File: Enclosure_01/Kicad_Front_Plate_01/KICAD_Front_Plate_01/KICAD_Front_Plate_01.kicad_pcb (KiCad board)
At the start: 2 copper layers, 124.8 x 50.9 mm, 0 parts

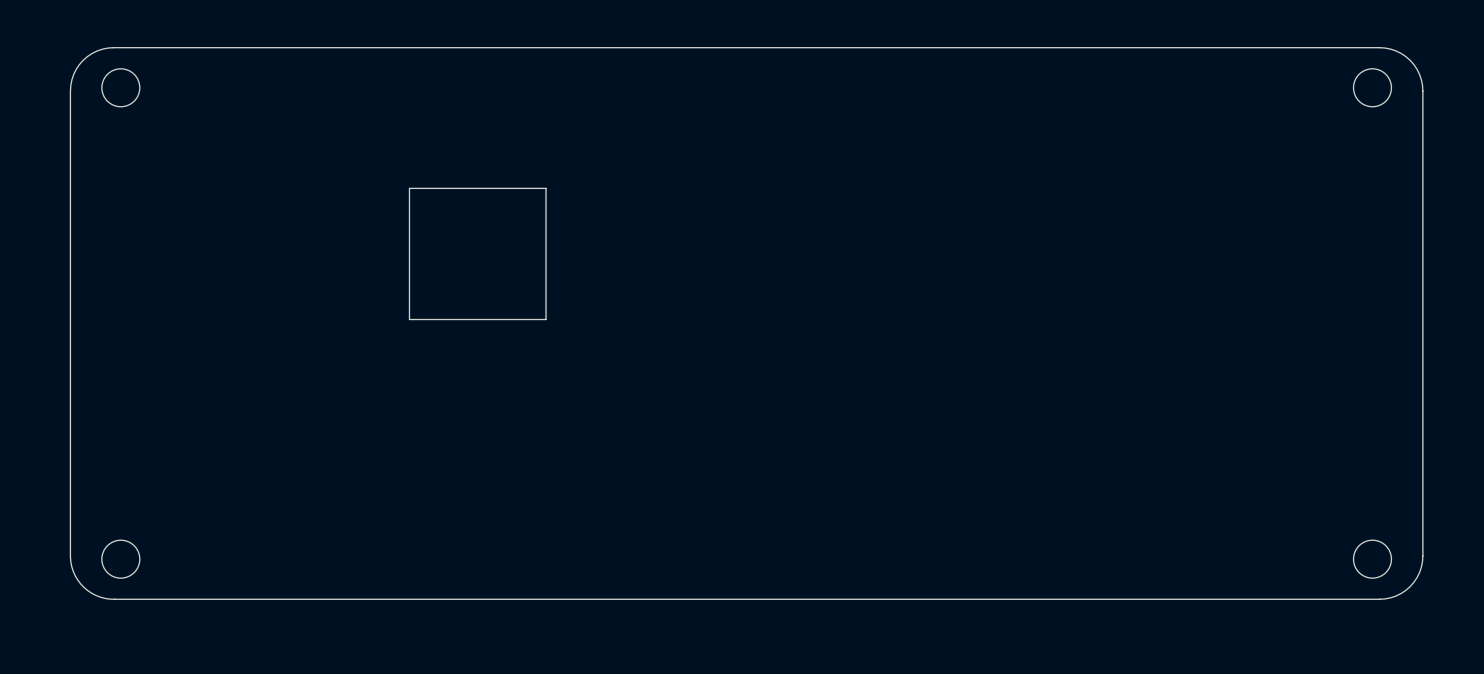
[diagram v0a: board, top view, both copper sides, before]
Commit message: Added masks to Kicad Front/back plates
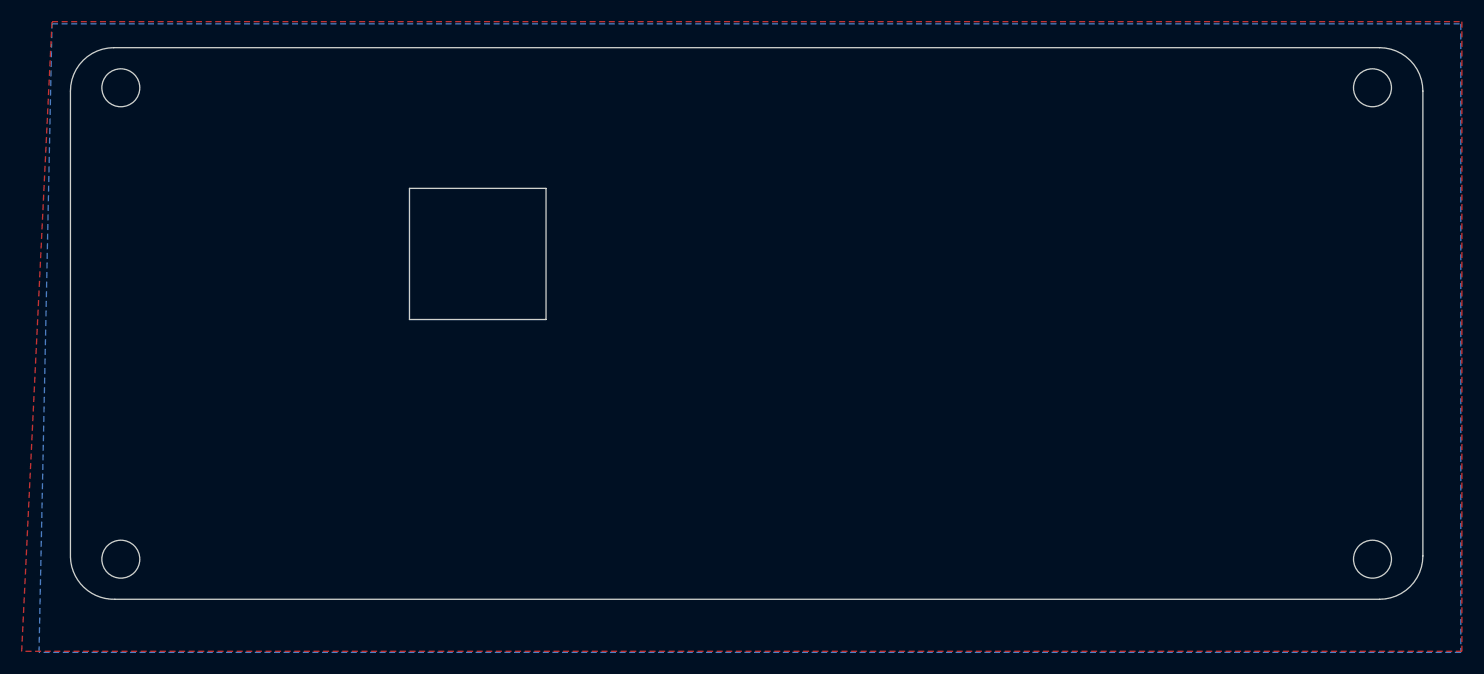
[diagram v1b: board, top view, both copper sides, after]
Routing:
- added copper zone on B.Cu, net (none)
- added copper zone on F.Cu, net (none)
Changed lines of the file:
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@@
   (gr_circle (center 120.15 3.7) (end 121.9 3.7) (layer Edge.Cuts) (width 0.05))
   (gr_circle (center 4.65 47.2) (end 6.4 47.2) (layer Edge.Cuts) (width 0.05))
+  (zone (net 0) (net_name "") (layer F.Cu) (hatch edge 0.508)
+    (connect_pads (clearance 0.508))
+    (min_thickness 0.254)
+    (fill yes (arc_segments 32) (thermal_gap 0.508) (thermal_bridge_width 0.508))
+    (polygon
+      (pts
+        (xy 128.4 55.7) (xy -4.5 55.7) (xy -1.7 -2.4) (xy 128.4 -2.4)
+      )
+    )
+  )
+  (zone (net 0) (net_name "") (layer B.Cu) (hatch edge 0.508)
+    (connect_pads (clearance 0.508))
+    (min_thickness 0.254)
+    (fill yes (arc_segments 32) (thermal_gap 0.508) (thermal_bridge_width 0.508))
+    (polygon
+      (pts
+        (xy 128.3 55.8) (xy -2.9 55.8) (xy -1.7 -2.2) (xy 128.3 -2.2)
+      )
+    )
+  )
 )

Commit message: Updated mounting holes for Copper Plane and Gerber
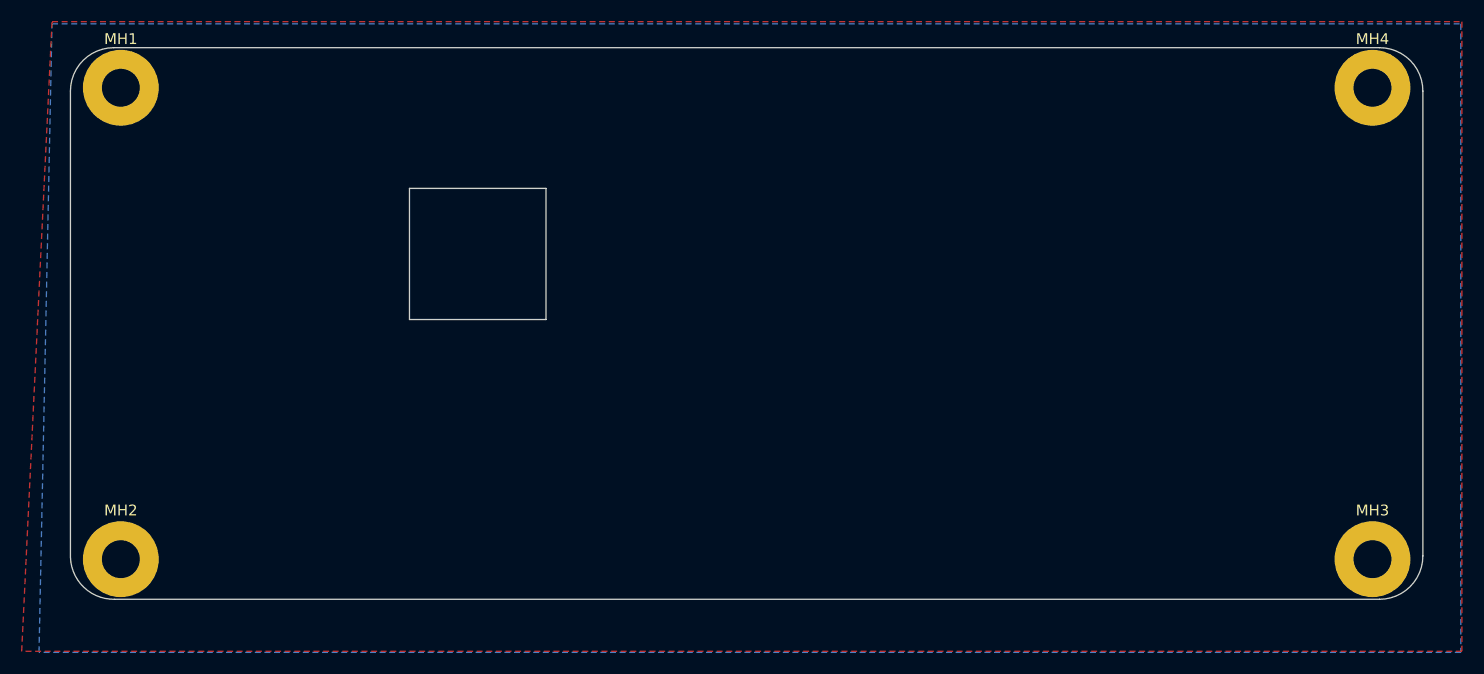
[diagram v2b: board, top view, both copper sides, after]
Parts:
- added MH1: MountingHole, MountingHole:MountingHole_3.5mm_Pad, F.Cu at (4.65, 3.70)
- added MH2: MountingHole, MountingHole:MountingHole_3.5mm_Pad, F.Cu at (4.65, 47.2)
- added MH3: MountingHole, MountingHole:MountingHole_3.5mm_Pad, F.Cu at (120.2, 47.2)
- added MH4: MountingHole, MountingHole:MountingHole_3.5mm_Pad, F.Cu at (120.2, 3.70)
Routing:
- net GND: track 0.00 -> 1.57 mm
- added copper zone on B.Cu, net GND
- added copper zone on F.Cu, net GND
- removed copper zone on B.Cu, net (none)
- removed copper zone on F.Cu, net (none)
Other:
- outline, holes or cut-outs redrawn
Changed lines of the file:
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@@
   (general
     (thickness 1.6)
-    (drawings 16)
-    (tracks 0)
+    (drawings 12)
+    (tracks 3)
     (zones 0)
-    (modules 0)
-    (nets 1)
+    (modules 4)
+    (nets 2)
   )
   (page A4)
@@
     (mod_text_size 1 1)
     (mod_text_width 0.15)
-    (pad_size 1.524 1.524)
-    (pad_drill 0.762)
+    (pad_size 7 7)
+    (pad_drill 3.5)
     (pad_to_mask_clearance 0)
     (aux_axis_origin 0 0)
@@
     (pcbplotparams
       (layerselection 0x010fc_ffffffff)
-      (usegerberextensions false)
-      (usegerberattributes true)
-      (usegerberadvancedattributes true)
-      (creategerberjobfile true)
+      (usegerberextensions true)
+      (usegerberattributes false)
+      (usegerberadvancedattributes false)
+      (creategerberjobfile false)
       (excludeedgelayer true)
       (linewidth 0.100000)
@@
       (psa4output false)
       (plotreference true)
-      (plotvalue true)
+      (plotvalue false)
       (plotinvisibletext false)
       (padsonsilk false)
-      (subtractmaskfromsilk false)
+      (subtractmaskfromsilk true)
       (outputformat 1)
       (mirror false)
@@
   )
   (net 0 "")
+  (net 1 GND)
   (net_class Default "This is the default net class."
     (clearance 0.2)
@@
     (uvia_dia 0.3)
     (uvia_drill 0.1)
+    (add_net GND)
+  )
+  (module MountingHole:MountingHole_3.5mm_Pad (layer F.Cu)
+    (at 4.65 3.7)
+    (descr "Mounting Hole 3.5mm")
+    (tags "mounting hole 3.5mm")
+    (attr virtual)
+    (fp_text reference MH1 (at 0 -4.5) (layer F.SilkS)
+      (effects (font (size 1 1) (thickness 0.15)))
+    )
+    (fp_text value MountingHole (at 0 4.5) (layer F.Fab)
+      (effects (font (size 1 1) (thickness 0.15)))
+    )
+    (fp_circle (center 0 0) (end 3.75 0) (layer F.CrtYd) (width 0.05))
+    (fp_circle (center 0 0) (end 3.5 0) (layer Cmts.User) (width 0.15))
+    (fp_text user %R (at 0.3 0) (layer F.Fab)
+      (effects (font (size 1 1) (thickness 0.15)))
+    )
+    (pad 1 thru_hole circle (at 0 0) (size 7 7) (drill 3.5) (layers *.Cu *.Mask)
+      (net 1 GND))
+  )
+  (module MountingHole:MountingHole_3.5mm_Pad (layer F.Cu)
+    (at 4.65 47.2)
+    (descr "Mounting Hole 3.5mm")
+    (tags "mounting hole 3.5mm")
+    (attr virtual)
+    (fp_text reference MH2 (at 0 -4.5) (layer F.SilkS)
+      (effects (font (size 1 1) (thickness 0.15)))
+    )
+    (fp_text value MountingHole (at 0 4.5) (layer F.Fab)
+      (effects (font (size 1 1) (thickness 0.15)))
+    )
+    (fp_circle (center 0 0) (end 3.75 0) (layer F.CrtYd) (width 0.05))
+    (fp_circle (center 0 0) (end 3.5 0) (layer Cmts.User) (width 0.15))
+    (fp_text user %R (at 0.3 0) (layer F.Fab)
+      (effects (font (size 1 1) (thickness 0.15)))
+    )
+    (pad 1 thru_hole circle (at 0 0) (size 7 7) (drill 3.5) (layers *.Cu *.Mask)
+      (net 1 GND))
+  )
+  (module MountingHole:MountingHole_3.5mm_Pad (layer F.Cu)
+    (at 120.15 47.2)
+    (descr "Mounting Hole 3.5mm")
+    (tags "mounting hole 3.5mm")
+    (attr virtual)
+    (fp_text reference MH3 (at 0 -4.5) (layer F.SilkS)
+      (effects (font (size 1 1) (thickness 0.15)))
+    )
+    (fp_text value MountingHole (at 0 4.5) (layer F.Fab)
+      (effects (font (size 1 1) (thickness 0.15)))
+    )
+    (fp_circle (center 0 0) (end 3.5 0) (layer Cmts.User) (width 0.15))
+    (fp_circle (center 0 0) (end 3.75 0) (layer F.CrtYd) (width 0.05))
+    (fp_text user %R (at 0.3 0) (layer F.Fab)
+      (effects (font (size 1 1) (thickness 0.15)))
+    )
+    (pad 1 thru_hole circle (at 0 0) (size 7 7) (drill 3.5) (layers *.Cu *.Mask)
+      (net 1 GND))
+  )
+  (module MountingHole:MountingHole_3.5mm_Pad (layer F.Cu)
+    (at 120.15 3.7)
+    (descr "Mounting Hole 3.5mm")
+    (tags "mounting hole 3.5mm")
+    (attr virtual)
+    (fp_text reference MH4 (at 0 -4.5) (layer F.SilkS)
+      (effects (font (size 1 1) (thickness 0.15)))
+    )
+    (fp_text value MountingHole (at 0 4.5) (layer F.Fab)
+      (effects (font (size 1 1) (thickness 0.15)))
+    )
+    (fp_circle (center 0 0) (end 3.5 0) (layer Cmts.User) (width 0.15))
+    (fp_circle (center 0 0) (end 3.75 0) (layer F.CrtYd) (width 0.05))
+    (fp_text user %R (at 0.3 0) (layer F.Fab)
+      (effects (font (size 1 1) (thickness 0.15)))
+    )
+    (pad 1 thru_hole circle (at 0 0) (size 7 7) (drill 3.5) (layers *.Cu *.Mask)
+      (net 1 GND))
   )
   (gr_line (start 31.285 25.085) (end 43.885 25.085) (layer Edge.Cuts) (width 0.05))
@@
   (gr_line (start 124.8 46.9) (end 124.8 4) (layer Edge.Cuts) (width 0.05))
   (gr_line (start 4 0) (end 120.8 0) (layer Edge.Cuts) (width 0.05))
-  (gr_circle (center 120.15 47.2) (end 121.9 47.2) (layer Edge.Cuts) (width 0.05))
-  (gr_circle (center 4.65 3.7) (end 6.4 3.7) (layer Edge.Cuts) (width 0.05))
   (gr_arc (start 4 46.9) (end 0 47) (angle -90) (layer Edge.Cuts) (width 0.05))
-  (gr_circle (center 120.15 3.7) (end 121.9 3.7) (layer Edge.Cuts) (width 0.05))
-  (gr_circle (center 4.65 47.2) (end 6.4 47.2) (layer Edge.Cuts) (width 0.05))
-  (zone (net 0) (net_name "") (layer F.Cu) (hatch edge 0.508)
+  (segment (start 4.65 46.193031) (end 4.301222 45.844253) (width 0.25) (layer F.Cu) (net 1))
+  (segment (start 4.301222 45.844253) (end 4.236612 45.862537) (width 0.25) (layer F.Cu) (net 1))
+  (segment (start 4.65 47.2) (end 4.65 46.193031) (width 0.25) (layer F.Cu) (net 1))
+  (zone (net 1) (net_name GND) (layer F.Cu) (hatch edge 0.508)
     (connect_pads (clearance 0.508))
     (min_thickness 0.254)
@@
     )
   )
-  (zone (net 0) (net_name "") (layer B.Cu) (hatch edge 0.508)
+  (zone (net 1) (net_name GND) (layer B.Cu) (hatch edge 0.508)
     (connect_pads (clearance 0.508))
     (min_thickness 0.254)
